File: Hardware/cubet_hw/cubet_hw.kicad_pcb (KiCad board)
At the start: 2 copper layers, 50 x 50 mm, 99 parts, among them J1 USB_B_Micro, J2 Conn_01x32, J3 Conn_01x32, J4 Conn_01x32, J8 Conn_01x04_Male, Q1 A03400A, Q2 A03400A, Q3 A03400A, Q4 A03400A, Q5 A03400A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

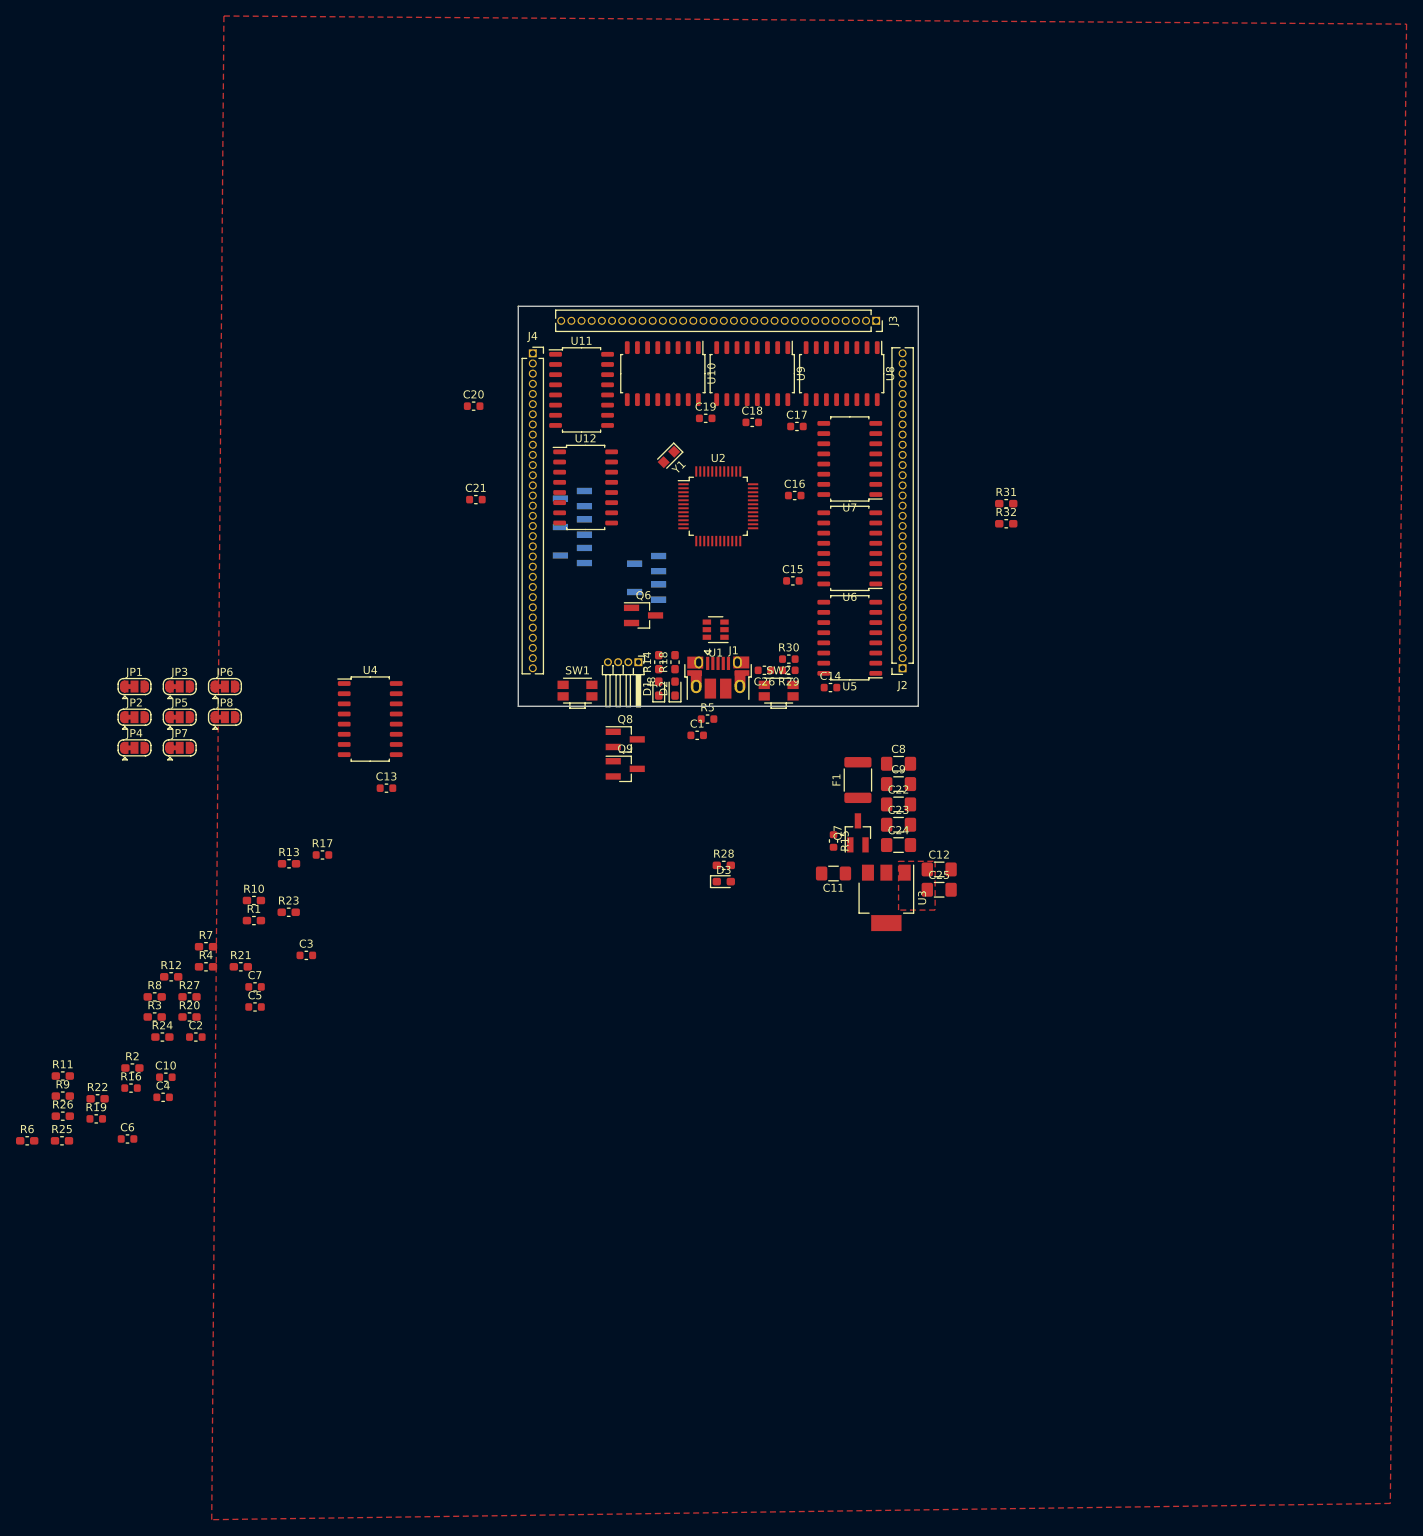
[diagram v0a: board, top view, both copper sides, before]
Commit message: bootloader flashed, ready to program
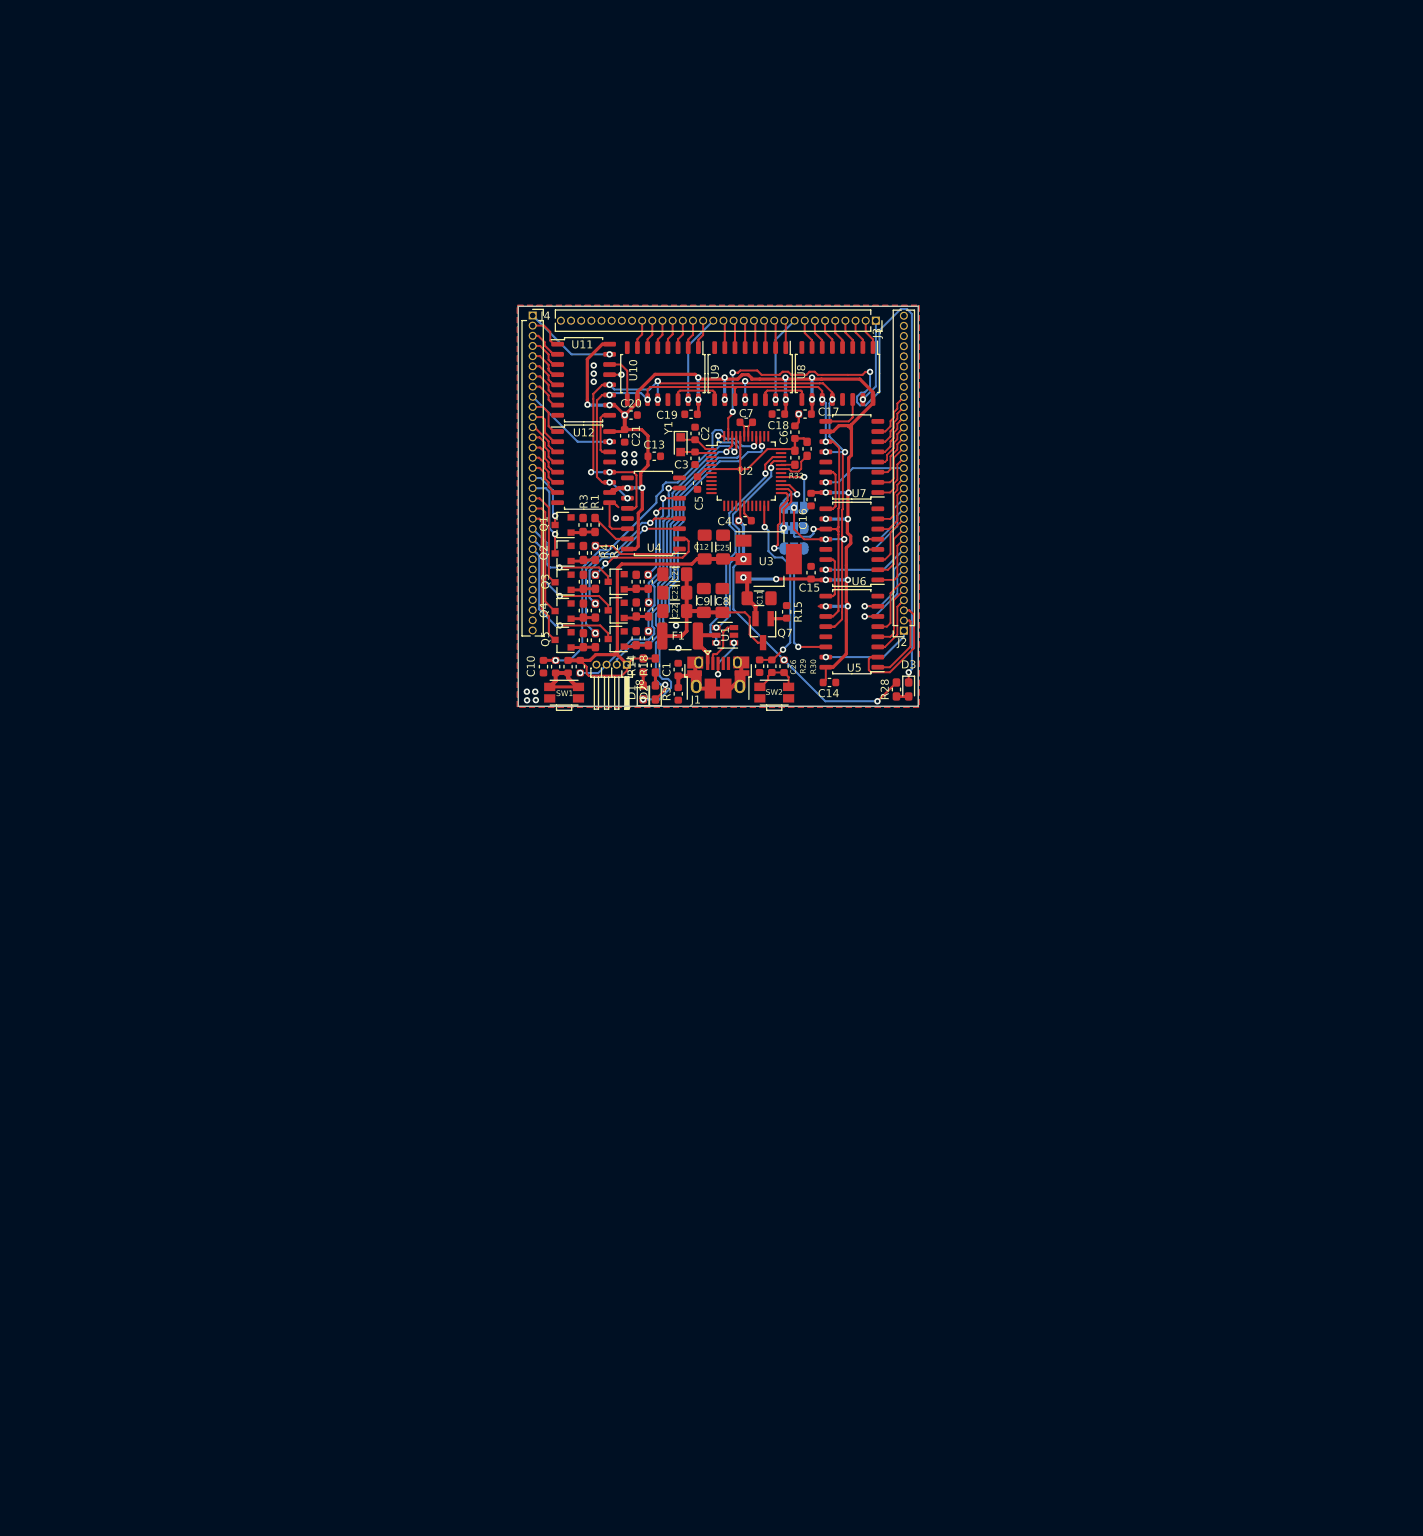
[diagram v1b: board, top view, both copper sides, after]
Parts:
- removed JP1, JP2, JP3, JP4, JP5, JP6, JP7, JP8: SolderJumper_3_Bridged12, Jumper:SolderJumper-3_P1.3mm_Bridged12_RoundedPad1.0x1.5mm
- removed R24, R25, R26, R27: 0R/NP, Resistor_SMD:R_0603_1608Metric_Pad1.05x0.95mm_HandSolder
- added JP10: SolderJumper_3_Bridged12, Jumper:SolderJumper-3_P1.3mm_Bridged12_RoundedPad1.0x1.5mm, B.Cu at (84.5, 77.7)
- added JP11: SolderJumper_3_Bridged12, Jumper:SolderJumper-3_P1.3mm_Bridged12_RoundedPad1.0x1.5mm, B.Cu at (84.5, 75.2)
- added JP9: SolderJumper_3_Bridged12, Jumper:SolderJumper-3_P1.3mm_Bridged12_RoundedPad1.0x1.5mm, B.Cu at (84.5, 80.3)
- Q1, Q2, Q3, Q4, Q5: footprint Package_TO_SOT_SMD:SOT-23_Handsoldering -> Package_TO_SOT_SMD:SOT-23; moved to F.Cu
- Q6, Q8, Q9: footprint Package_TO_SOT_SMD:SOT-23_Handsoldering -> Package_TO_SOT_SMD:SOT-23
- moved C6 121.5 mm to (84.6, 65.7), turned to 270 degrees
- moved C4 102.4 mm to (78.3, 76.8), turned to 180 degrees
- moved R6 99.6 mm to (59.6, 84.4), turned to 90 degrees
- moved C2 97.9 mm to (72.1, 65.9), turned to 270 degrees
- moved R11 95.8 mm to (66.2, 84.4), turned to 90 degrees
- moved C7 93.5 mm to (78.5, 64.5)
- moved R22 91.0 mm to (64.8, 87.9), turned to 270 degrees
- moved R9 89.0 mm to (58.1, 88.0), turned to 270 degrees
- moved R2 86.6 mm to (59.6, 80.8), turned to 90 degrees
- moved C5 85.7 mm to (72.4, 72.1), turned to 90 degrees
- moved R19 81.7 mm to (56.2, 95.0), turned to 270 degrees
- moved R3 81.5 mm to (58.1, 77.3), turned to 270 degrees
- moved C3 78.9 mm to (72.1, 69.0), turned to 90 degrees
- moved R16 77.0 mm to (57.8, 95.0), turned to 90 degrees
- moved R20 76.7 mm to (66.3, 87.9), turned to 90 degrees
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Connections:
- R1 pad 2: Net-(JP1-Pad2) -> CTRL_ROW_0_SHIFT
- R10 pad 2: Net-(JP5-Pad2) -> CTRL_ROW_4_SHIFT
- R11 pad 2: Net-(JP6-Pad2) -> CTRL_ROW_5_SHIFT
- R2 pad 2: Net-(JP2-Pad2) -> CTRL_ROW_1_SHIFT
- R20 pad 2: Net-(JP7-Pad2) -> CTRL_ROW_6_SHIFT
- R21 pad 2: Net-(JP8-Pad2) -> CTRL_ROW_7_SHIFT
- R6 pad 2: Net-(JP3-Pad2) -> CTRL_ROW_2_SHIFT
- R7 pad 2: Net-(JP4-Pad2) -> CTRL_ROW_3_SHIFT
- U10 pad 14: SHIFT_DATA_5 -> SHIFT_DATA_4
- U11 pad 14: SHIFT_DATA_6 -> SHIFT_DATA_5
- U12 pad 14: SHIFT_DATA_7 -> SHIFT_DATA_6
- U2 pad 29: Net-(U2-Pad29) -> LATCH_TCC
- U2 pad 34: D+_USB -> D+_UC
- U4 pad 10: Net-(R24-Pad1) -> +5V
- U4 pad 13: Net-(R25-Pad1) -> GND
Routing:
- net +5V: track 0.00 -> 169.4 mm, vias 0 -> 23
- net +3V3: track 0.00 -> 116.1 mm, vias 0 -> 4
- net SHIFT_LATCH: track 0.00 -> 101.2 mm, vias 0 -> 13
- net DEBUG_LED: track 0.00 -> 94.2 mm, vias 0 -> 4
- net SHIFT_CLK: track 0.00 -> 85.7 mm, vias 0 -> 7
- net ~RESET~: track 0.00 -> 48.5 mm, vias 0 -> 2
- net PA27_TX_LED: track 0.00 -> 44.4 mm, vias 0 -> 2
- net PB03_RX_LED: track 0.00 -> 43.1 mm, vias 0 -> 2
- net SWCLK: track 0.00 -> 42.6 mm, vias 0 -> 2
- net SWDIO: track 0.00 -> 36.6 mm, vias 0 -> 1
- net D+_UC: track 0.00 -> 28.8 mm, vias 0 -> 2
- net D-_UC: track 0.00 -> 25.5 mm, vias 0 -> 2
- net Net-(C22-Pad1): track 0.00 -> 23.8 mm
- net BUTTON_0: track 0.00 -> 23.7 mm, vias 0 -> 2
- net CTRL_ROW_4_SHIFT: track 0.00 -> 23.1 mm, vias 0 -> 2
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- added copper zone on F.Cu, net (none)
- added copper zone on B.Cu, net GND
- removed copper zone on F.Cu, net +3V3
